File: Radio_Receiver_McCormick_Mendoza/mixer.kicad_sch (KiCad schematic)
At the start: 32 parts, among them J13 I_0, J14 I_180, J15 Q_90, J16 Q_270, J17 I_OUT, J18 Conn_01x02_Female, J19 Conn_01x02_Female, J20 Q_OUT, U11 INA821ID, U8 SN74CBT3253CDBR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

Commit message: Isolated filter switching MUX from digital control
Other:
- moved on the sheet: J18, J19
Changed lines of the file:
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@@
 	)
 	(junction
-		(at 176.53 54.61)
+		(at 138.43 43.18)
 		(diameter 0)
 		(color 0 0 0 0)
 	)
 	(junction
-		(at 187.96 133.35)
+		(at 134.62 91.44)
 		(diameter 0)
 		(color 0 0 0 0)
 	)
 	(junction
-		(at 138.43 43.18)
+		(at 261.62 59.69)
 		(diameter 0)
 		(color 0 0 0 0)
 	)
 	(junction
-		(at 134.62 91.44)
+		(at 176.53 54.61)
 		(diameter 0)
 		(color 0 0 0 0)
 	)
 	(junction
-		(at 261.62 59.69)
+		(at 186.69 71.12)
 		(diameter 0)
 		(color 0 0 0 0)
@@
 	)
 	(junction
-		(at 177.8 116.84)
+		(at 194.31 116.84)
 		(diameter 0)
 		(color 0 0 0 0)
 	)
 	(junction
-		(at 194.31 116.84)
+		(at 137.16 93.98)
 		(diameter 0)
 		(color 0 0 0 0)
 	)
 	(junction
-		(at 137.16 93.98)
+		(at 187.96 133.35)
 		(diameter 0)
 		(color 0 0 0 0)
@@
 	)
 	(junction
+		(at 177.8 116.84)
+		(diameter 0)
+		(color 0 0 0 0)
+	)
+	(junction
 		(at 203.2 71.12)
 		(diameter 0)
@@
 	)
 	(junction
-		(at 186.69 71.12)
-		(diameter 0)
-		(color 0 0 0 0)
-	)
-	(junction
 		(at 139.7 83.82)
 		(diameter 0)
@@
 	(wire
 		(pts
-			(xy 154.94 68.58) (xy 154.94 54.61)
+			(xy 172.72 62.23) (xy 172.72 54.61)
 		)
 		(stroke
@@
 	(wire
 		(pts
+			(xy 173.99 125.73) (xy 173.99 133.35)
+		)
+		(stroke
+			(width 0)
+			(type default)
+		)
+	)
+	(wire
+		(pts
 			(xy 137.16 143.51) (xy 168.91 143.51)
 		)
@@
 	(wire
 		(pts
-			(xy 154.94 130.81) (xy 156.21 130.81)
+			(xy 172.72 123.19) (xy 173.99 123.19)
 		)
 		(stroke
@@
 	(wire
 		(pts
+			(xy 172.72 64.77) (xy 172.72 71.12)
+		)
+		(stroke
+			(width 0)
+			(type default)
+		)
+	)
+	(wire
+		(pts
 			(xy 245.11 130.81) (xy 246.38 130.81)
 		)
@@
 	(wire
 		(pts
-			(xy 153.67 71.12) (xy 186.69 71.12)
+			(xy 167.64 64.77) (xy 172.72 64.77)
 		)
 		(stroke
@@
 	(wire
 		(pts
-			(xy 154.94 54.61) (xy 176.53 54.61)
+			(xy 172.72 54.61) (xy 176.53 54.61)
 		)
 		(stroke
@@
 	(wire
 		(pts
+			(xy 172.72 71.12) (xy 186.69 71.12)
+		)
+		(stroke
+			(width 0)
+			(type default)
+		)
+	)
+	(wire
+		(pts
 			(xy 232.41 143.51) (xy 232.41 128.27)
 		)
@@
 	(wire
 		(pts
+			(xy 173.99 133.35) (xy 187.96 133.35)
+		)
+		(stroke
+			(width 0)
+			(type default)
+		)
+	)
+	(wire
+		(pts
 			(xy 261.62 115.57) (xy 271.78 115.57)
 		)
@@
 	(wire
 		(pts
-			(xy 153.67 68.58) (xy 154.94 68.58)
+			(xy 167.64 62.23) (xy 172.72 62.23)
 		)
 		(stroke
@@
 	(wire
 		(pts
-			(xy 156.21 130.81) (xy 156.21 116.84)
+			(xy 173.99 123.19) (xy 173.99 116.84)
 		)
 		(stroke
@@
 	(wire
 		(pts
-			(xy 154.94 133.35) (xy 187.96 133.35)
+			(xy 172.72 125.73) (xy 173.99 125.73)
 		)
 		(stroke
@@
 	(wire
 		(pts
-			(xy 156.21 116.84) (xy 177.8 116.84)
+			(xy 173.99 116.84) (xy 177.8 116.84)
 		)
 		(stroke
@@
 	(symbol
 		(lib_id "Connector:Conn_01x02_Female")
-		(at 149.86 133.35 180)
+		(at 167.64 125.73 180)
 		(unit 1)
 		(body_style 1)
@@
 		(dnp no)
 		(property "Reference" "J19"
-			(at 146.304 132.842 0)
+			(at 164.084 125.222 0)
 			(show_name no)
 			(do_not_autoplace no)
@@
 		)
 		(property "Value" "Conn_01x02_Female"
-			(at 147.574 135.382 0)
+			(at 165.354 127.762 0)
 			(show_name no)
 			(do_not_autoplace no)
@@
 		)
 		(property "Footprint" "Connector_PinSocket_2.54mm:PinSocket_1x02_P2.54mm_Vertical"
-			(at 149.86 133.35 0)
+			(at 167.64 125.73 0)
 			(hide yes)
 			(show_name no)
@@
 		)
 		(property "Datasheet" "~"
-			(at 149.86 133.35 0)
+			(at 167.64 125.73 0)
 			(hide yes)
 			(show_name no)
@@
 		)
 		(property "Description" ""
-			(at 149.86 133.35 0)
+			(at 167.64 125.73 0)
 			(show_name no)
 			(do_not_autoplace no)
@@
 	(symbol
 		(lib_id "Connector:Conn_01x02_Female")
-		(at 148.59 71.12 180)
+		(at 162.56 64.77 180)
 		(unit 1)
 		(body_style 1)
@@
 		(dnp no)
 		(property "Reference" "J18"
-			(at 145.034 70.612 0)
+			(at 159.004 64.262 0)
 			(show_name no)
 			(do_not_autoplace no)
@@
 		)
 		(property "Value" "Conn_01x02_Female"
-			(at 146.304 73.152 0)
+			(at 160.274 66.802 0)
 			(show_name no)
 			(do_not_autoplace no)
@@
 		)
 		(property "Footprint" "Connector_PinSocket_2.54mm:PinSocket_1x02_P2.54mm_Vertical"
-			(at 148.59 71.12 0)
+			(at 162.56 64.77 0)
 			(hide yes)
 			(show_name no)
@@
 		)
 		(property "Datasheet" "~"
-			(at 148.59 71.12 0)
+			(at 162.56 64.77 0)
 			(hide yes)
 			(show_name no)
@@
 		)
 		(property "Description" ""
-			(at 148.59 71.12 0)
+			(at 162.56 64.77 0)
 			(show_name no)
 			(do_not_autoplace no)

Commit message: Added digital power regulator
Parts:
- removed C19, C21: 100nF, PCM_JLCPCB:C_1206, symbol Device:C
- added C62, C63: 100nF, PCM_JLCPCB:C_1206, symbol Device:C
- C14, C15, C9: Manufacturer Samsung Electro-Mechanics -> (none)
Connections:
- net GND: now also C62.2, C63.2
- net VDDA/2: now also C62.1, C63.1
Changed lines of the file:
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@@
 	)
 	(symbol
-		(lib_id "Device:C")
-		(at 246.38 138.43 0)
-		(unit 1)
-		(body_style 1)
-		(exclude_from_sim no)
-		(in_bom yes)
-		(on_board yes)
-		(in_pos_files yes)
-		(dnp no)
-		(fields_autoplaced yes)
-		(property "Reference" "C19"
-			(at 250.19 137.1599 0)
-			(show_name no)
-			(do_not_autoplace no)
-			(effects
-				(font
-					(size 1.27 1.27)
-				)
-				(justify left)
-			)
-		)
-		(property "Value" "100nF"
-			(at 250.19 139.6999 0)
-			(show_name no)
-			(do_not_autoplace no)
-			(effects
-				(font
-					(size 1.27 1.27)
-				)
-				(justify left)
-			)
-		)
-		(property "Footprint" "PCM_JLCPCB:C_1206"
-			(at 247.3452 142.24 0)
-			(hide yes)
-			(show_name no)
-			(do_not_autoplace no)
-			(effects
-				(font
-					(size 1.27 1.27)
-				)
-			)
-		)
-		(property "Datasheet" "https://jlcpcb.com/partdetail/HRE-CSA1206C0G104J500NT/C52147198"
-			(at 246.38 138.43 0)
-			(hide yes)
-			(show_name no)
-			(do_not_autoplace no)
-			(effects
-				(font
-					(size 1.27 1.27)
-				)
-			)
-		)
-		(property "Description" "100nF 50V C0G ±5% 1206 Multilayer Ceramic Capacitors MLCC - SMD/SMT ROHS"
-			(at 246.38 138.43 0)
-			(hide yes)
-			(show_name no)
-			(do_not_autoplace no)
-			(effects
-				(font
-					(size 1.27 1.27)
-				)
-			)
-		)
-		(pin "2"
-		)
-		(pin "1"
-		)
-		(instances
-			(project "Radio_Receiver_McCormick_Mendoza"
-				(path "/f31d31ab-6846-4f3a-92b1-aa5a6a13373f/132a78a3-63a8-4709-a5ba-2b34eb7966d9"
-					(reference "C19")
-					(unit 1)
-				)
-			)
-		)
-	)
-	(symbol
 		(lib_id "Jumper:Jumper_2_Open")
 		(at 198.12 63.5 0)
@@
 			)
 		)
-		(property "Manufacturer" "Samsung Electro-Mechanics"
-			(at 63.5 64.77 0)
-			(hide yes)
-			(show_name no)
-			(do_not_autoplace no)
-			(effects
-				(font
-					(size 1.27 1.27)
-				)
-			)
-		)
 		(property "Part" "CL21B104KCFNNNE"
 			(at 63.5 64.77 0)
@@
 	)
 	(symbol
-		(lib_id "Device:C")
-		(at 245.11 74.93 0)
-		(unit 1)
-		(body_style 1)
-		(exclude_from_sim no)
-		(in_bom yes)
-		(on_board yes)
-		(in_pos_files yes)
-		(dnp no)
-		(fields_autoplaced yes)
-		(property "Reference" "C21"
-			(at 248.92 73.6599 0)
-			(show_name no)
-			(do_not_autoplace no)
-			(effects
-				(font
-					(size 1.27 1.27)
-				)
-				(justify left)
-			)
-		)
-		(property "Value" "100nF"
-			(at 248.92 76.1999 0)
-			(show_name no)
-			(do_not_autoplace no)
-			(effects
-				(font
-					(size 1.27 1.27)
-				)
-				(justify left)
-			)
-		)
-		(property "Footprint" "PCM_JLCPCB:C_1206"
-			(at 246.0752 78.74 0)
-			(hide yes)
-			(show_name no)
-			(do_not_autoplace no)
-			(effects
-				(font
-					(size 1.27 1.27)
-				)
-			)
-		)
-		(property "Datasheet" "https://jlcpcb.com/partdetail/HRE-CSA1206C0G104J500NT/C52147198"
-			(at 245.11 74.93 0)
-			(hide yes)
-			(show_name no)
-			(do_not_autoplace no)
-			(effects
-				(font
-					(size 1.27 1.27)
-				)
-			)
-		)
-		(property "Description" "100nF 50V C0G ±5% 1206 Multilayer Ceramic Capacitors MLCC - SMD/SMT ROHS"
-			(at 245.11 74.93 0)
-			(hide yes)
-			(show_name no)
-			(do_not_autoplace no)
-			(effects
-				(font
-					(size 1.27 1.27)
-				)
-			)
-		)
-		(pin "2"
-		)
-		(pin "1"
-		)
-		(instances
-			(project "Radio_Receiver_McCormick_Mendoza"
-				(path "/f31d31ab-6846-4f3a-92b1-aa5a6a13373f/132a78a3-63a8-4709-a5ba-2b34eb7966d9"
-					(reference "C21")
-					(unit 1)
-				)
-			)
-		)
-	)
-	(symbol
 		(lib_id "Connector:Conn_01x02_Female")
 		(at 167.64 125.73 180)
@@
 	)
 	(symbol
+		(lib_id "Device:C")
+		(at 246.38 138.43 0)
+		(unit 1)
+		(body_style 1)
+		(exclude_from_sim no)
+		(in_bom yes)
+		(on_board yes)
+		(in_pos_files yes)
+		(dnp no)
+		(fields_autoplaced yes)
+		(property "Reference" "C63"
+			(at 250.19 137.1599 0)
+			(show_name no)
+			(do_not_autoplace no)
+			(effects
+				(font
+					(size 1.27 1.27)
+				)
+				(justify left)
+			)
+		)
+		(property "Value" "100nF"
+			(at 250.19 139.6999 0)
+			(show_name no)
+			(do_not_autoplace no)
+			(effects
+				(font
+					(size 1.27 1.27)
+				)
+				(justify left)
+			)
+		)
+		(property "Footprint" "PCM_JLCPCB:C_1206"
+			(at 247.3452 142.24 0)
+			(hide yes)
+			(show_name no)
+			(do_not_autoplace no)
+			(effects
+				(font
+					(size 1.27 1.27)
+				)
+			)
+		)
+		(property "Datasheet" "https://jlcpcb.com/partdetail/HRE-CSA1206C0G104J500NT/C52147198"
+			(at 246.38 138.43 0)
+			(hide yes)
+			(show_name no)
+			(do_not_autoplace no)
+			(effects
+				(font
+					(size 1.27 1.27)
+				)
+			)
+		)
+		(property "Description" "100nF 50V C0G ±5% 1206 Multilayer Ceramic Capacitors MLCC - SMD/SMT ROHS"
+			(at 246.38 138.43 0)
+			(hide yes)
+			(show_name no)
+			(do_not_autoplace no)
+			(effects
+				(font
+					(size 1.27 1.27)
+				)
+			)
+		)
+		(property "LCSC" "C52147198"
+			(at 246.38 138.43 0)
+			(hide yes)
+			(show_name no)
+			(do_not_autoplace no)
+			(effects
+				(font
+					(size 1.27 1.27)
+				)
+			)
+		)
+		(pin "2"
+		)
+		(pin "1"
+		)
+		(instances
+			(project "Radio_Receiver_McCormick_Mendoza"
+				(path "/f31d31ab-6846-4f3a-92b1-aa5a6a13373f/132a78a3-63a8-4709-a5ba-2b34eb7966d9"
+					(reference "C63")
+					(unit 1)
+				)
+			)
+		)
+	)
+	(symbol
 		(lib_id "power:GND")
 		(at 115.57 106.68 0)
@@
 			)
 		)
-		(property "Manufacturer" "Samsung Electro-Mechanics"
-			(at 245.11 49.53 0)
-			(hide yes)
-			(show_name no)
-			(do_not_autoplace no)
-			(effects
-				(font
-					(size 1.27 1.27)
-				)
-			)
-		)
 		(property "Part" "CL21B104KCFNNNE"
 			(at 245.11 49.53 0)
@@
 	(symbol
 		(lib_id "Device:C")
+		(at 245.11 74.93 0)
+		(unit 1)
+		(body_style 1)
+		(exclude_from_sim no)
+		(in_bom yes)
+		(on_board yes)
+		(in_pos_files yes)
+		(dnp no)
+		(fields_autoplaced yes)
+		(property "Reference" "C62"
+			(at 248.92 73.6599 0)
+			(show_name no)
+			(do_not_autoplace no)
+			(effects
+				(font
+					(size 1.27 1.27)
+				)
+				(justify left)
+			)
+		)
+		(property "Value" "100nF"
+			(at 248.92 76.1999 0)
+			(show_name no)
+			(do_not_autoplace no)
+			(effects
+				(font
+					(size 1.27 1.27)
+				)
+				(justify left)
+			)
+		)
+		(property "Footprint" "PCM_JLCPCB:C_1206"
+			(at 246.0752 78.74 0)
+			(hide yes)
+			(show_name no)
+			(do_not_autoplace no)
+			(effects
+				(font
+					(size 1.27 1.27)
+				)
+			)
+		)
+		(property "Datasheet" "https://jlcpcb.com/partdetail/HRE-CSA1206C0G104J500NT/C52147198"
+			(at 245.11 74.93 0)
+			(hide yes)
+			(show_name no)
+			(do_not_autoplace no)
+			(effects
+				(font
+					(size 1.27 1.27)
+				)
+			)
+		)
+		(property "Description" "100nF 50V C0G ±5% 1206 Multilayer Ceramic Capacitors MLCC - SMD/SMT ROHS"
+			(at 245.11 74.93 0)
+			(hide yes)
+			(show_name no)
+			(do_not_autoplace no)
+			(effects
+				(font
+					(size 1.27 1.27)
+				)
+			)
+		)
+		(property "LCSC" "C52147198"
+			(at 245.11 74.93 0)
+			(hide yes)
+			(show_name no)
+			(do_not_autoplace no)
+			(effects
+				(font
+					(size 1.27 1.27)
+				)
+			)
+		)
+		(pin "2"
+		)
+		(pin "1"
+		)
+		(instances
+			(project "Radio_Receiver_McCormick_Mendoza"
+				(path "/f31d31ab-6846-4f3a-92b1-aa5a6a13373f/132a78a3-63a8-4709-a5ba-2b34eb7966d9"
+					(reference "C62")
+					(unit 1)
+				)
+			)
+		)
+	)
+	(symbol
+		(lib_id "Device:C")
 		(at 138.43 46.99 0)
 		(unit 1)
@@
 			(at 246.38 113.03 0)
 			(hide yes)
-			(show_name no)
-			(do_not_autoplace no)
-			(effects
-				(font
-					(size 1.27 1.27)
-				)
-			)
-		)
-		(property "Manufacturer" "Samsung Electro-Mechanics"
-			(at 246.38 113.03 0)
-			(hide yes)

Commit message: Integrated signal path modules
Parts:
- removed C10, C11, C17, C18: 100p, Capacitor_THT:C_Disc_D5.0mm_W2.5mm_P2.50mm, symbol Device:C
- added C69, C79, C81, C82: 10nF, PCM_JLCPCB:C_0805, symbol Device:C
- J17: value I_OUT -> I_RAW
- J20: value Q_OUT -> Q_RAW
- R11, R14: LCSC (none) -> C861188
- R12, R15: LCSC (none) -> C861486
- R13, R16: LCSC (none) -> C861101
- U11, U9: LCSC (none) -> C2060822
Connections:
- net 00 = 0°: now also C69.2
- net 01 = 270°: now also C82.2
- net 10 = 90°: now also C81.2
- net 11 = 180°: now also C79.2
- net GND: now also C69.1, C79.1, C81.1, C82.1

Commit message: Finalized Pico connections and added indicator LEDs
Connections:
- net BPF_OUT1 renamed RF_IN1
- net BPF_OUT2 renamed RF_IN2

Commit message: Added transformer footprint and datasheet
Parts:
- U8: LCSC (none) -> C2674583; Price (none) -> 3.5033USD
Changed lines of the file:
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@@
+			)
+		)
+		(property "LCSC" "C2674583"
+			(at 95.25 88.9 0)
+			(hide yes)
+			(show_name no)
+			(do_not_autoplace no)
+			(effects
+				(font
+					(size 1.27 1.27)
+				)
+			)
+		)
+		(property "Price" "3.5033USD"
+			(at 95.25 88.9 0)
+			(hide yes)
+			(show_name no)
+			(do_not_autoplace no)
+			(effects
+				(font
+					(size 1.27 1.27)
+				)
 			)
 		)

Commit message: Added MicroSD card and verified footprints
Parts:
- JP2, JP3, JP4, JP7, JP8, JP9: footprint (none) -> Jumper:SolderJumper-2_P1.3mm_Open_RoundedPad1.0x1.5mm
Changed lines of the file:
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@@
 			)
 		)
-		(property "Footprint" ""
+		(property "Footprint" "Jumper:SolderJumper-2_P1.3mm_Open_RoundedPad1.0x1.5mm"
 			(at 182.88 125.73 0)
 			(hide yes)
@@
 			)
 		)
-		(property "Footprint" ""
+		(property "Footprint" "Jumper:SolderJumper-2_P1.3mm_Open_RoundedPad1.0x1.5mm"
 			(at 198.12 63.5 0)
 			(hide yes)
@@
 			)
 		)
-		(property "Footprint" ""
+		(property "Footprint" "Jumper:SolderJumper-2_P1.3mm_Open_RoundedPad1.0x1.5mm"
 			(at 214.63 63.5 0)
 			(hide yes)
@@
 			)
 		)
-		(property "Footprint" ""
+		(property "Footprint" "Jumper:SolderJumper-2_P1.3mm_Open_RoundedPad1.0x1.5mm"
 			(at 199.39 125.73 0)
 			(hide yes)
@@
 			)
 		)
-		(property "Footprint" ""
+		(property "Footprint" "Jumper:SolderJumper-2_P1.3mm_Open_RoundedPad1.0x1.5mm"
 			(at 215.9 125.73 0)
 			(hide yes)
@@
 		(property "Description" ""
 			(at 190.5 83.82 0)
+			(hide yes)
 			(show_name no)
 			(do_not_autoplace no)
@@
 			)
 		)
-		(property "Footprint" ""
+		(property "Footprint" "Jumper:SolderJumper-2_P1.3mm_Open_RoundedPad1.0x1.5mm"
 			(at 181.61 63.5 0)
 			(hide yes)

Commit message: Updated footprints
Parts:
- U11, U9: footprint import_footprint:SOIC127P600X175-8N -> INA821ID:D0008A_N
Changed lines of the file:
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@@
 	(wire
 		(pts
-			(xy 238.76 50.8) (xy 238.76 49.53)
-		)
-		(stroke
-			(width 0)
-			(type default)
-		)
-	)
-	(wire
-		(pts
 			(xy 219.71 71.12) (xy 228.6 71.12)
 		)
@@
 			)
 		)
-		(property "Footprint" "import_footprint:SOIC127P600X175-8N"
+		(property "Footprint" "INA821ID:D0008A_N"
 			(at 242.57 123.19 0)
 			(hide yes)
@@
 			)
 		)
-		(property "Footprint" "import_footprint:SOIC127P600X175-8N"
+		(property "Footprint" "INA821ID:D0008A_N"
 			(at 241.3 59.69 0)
 			(hide yes)

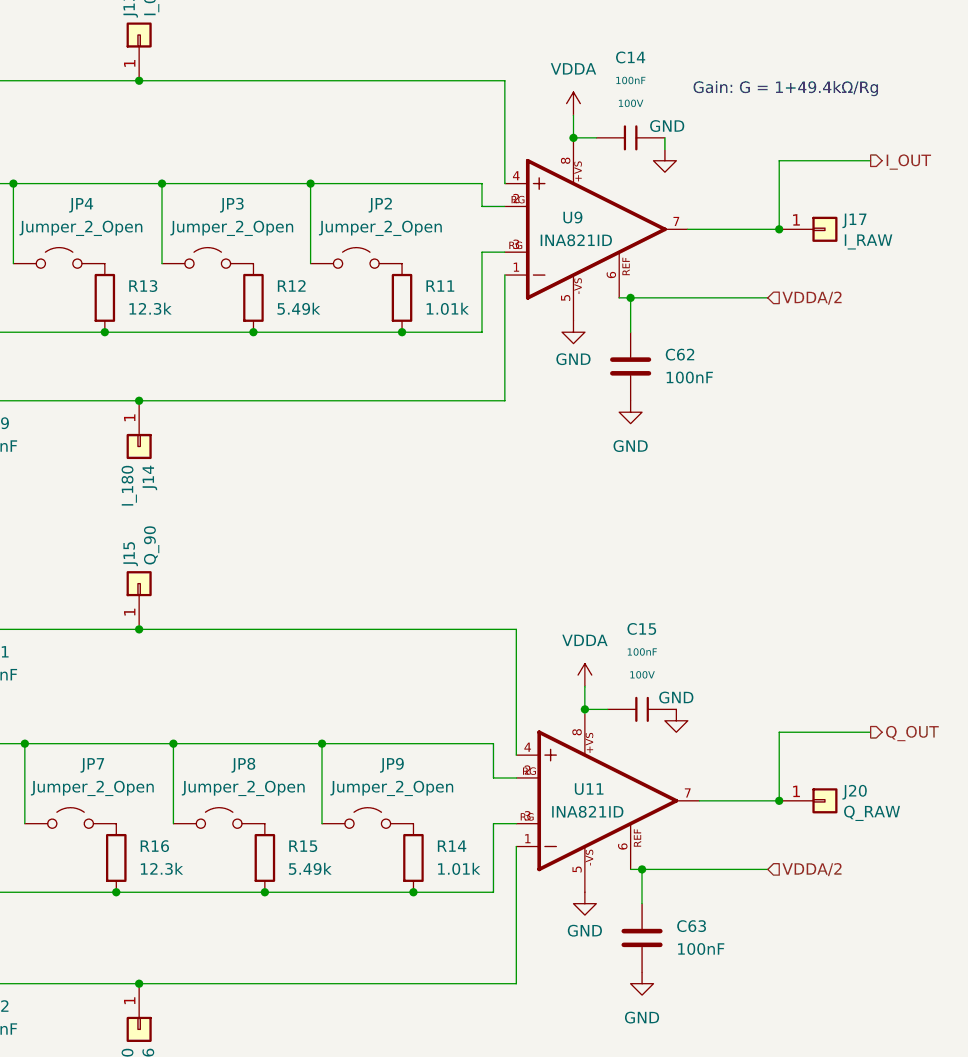
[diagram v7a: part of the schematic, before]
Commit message: Routed antenna and isolated GNDA
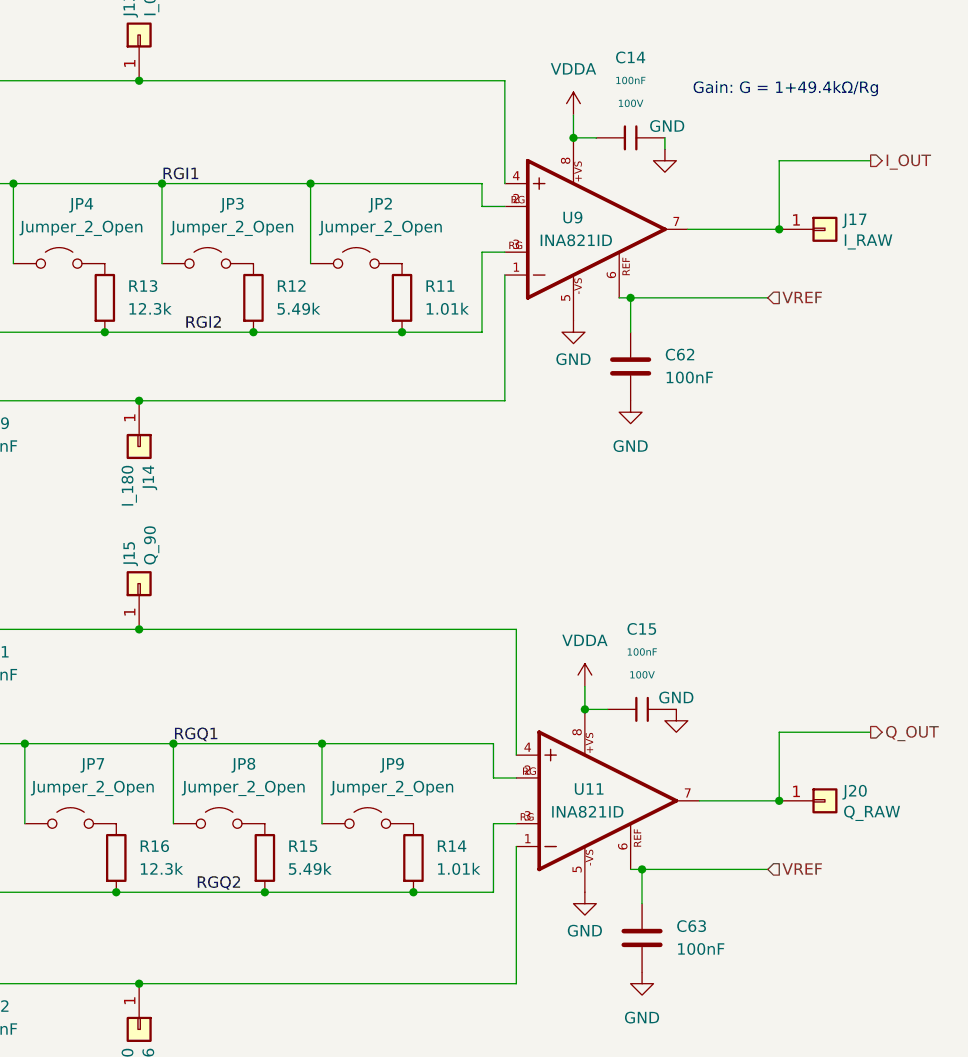
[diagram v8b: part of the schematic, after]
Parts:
- U11, U9: footprint INA821ID:D0008A_N -> Reciever_Parts:D0008A_N
- U8: footprint SN74CBT3253CDBR_1-4_MUX:DB0016A_N -> Reciever_Parts:DB0016A_N
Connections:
- net RGQ2: now reaches J19.1 (Pin_1), R14.2, R15.2, R16.2, U11.3 (RG1)
- net RGQ1: now reaches J19.2 (Pin_2), JP7.1 (A), JP8.1 (A), JP9.1 (A), U11.2 (RG)
- net RGI1: now reaches J18.2 (Pin_2), JP2.1 (A), JP3.1 (A), JP4.1 (A), U9.2 (RG)
- net RGI2: now reaches J18.1 (Pin_1), R11.2, R12.2, R13.2, U9.3 (RG1)
- net VDDA/2 renamed VREF
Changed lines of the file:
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@@
 		)
 	)
+	(label "RGI1"
+		(at 193.04 54.61 0)
+		(effects
+			(font
+				(size 1.27 1.27)
+			)
+			(justify left bottom)
+		)
+	)
 	(label "00 = 0°"
 		(at 125.73 76.2 180)
@@
 		)
 	)
+	(label "RGQ1"
+		(at 194.31 116.84 0)
+		(effects
+			(font
+				(size 1.27 1.27)
+			)
+			(justify left bottom)
+		)
+	)
 	(label "11 = 180°"
 		(at 156.21 78.74 180)
@@
 		)
 	)
+	(label "RGI2"
+		(at 195.58 71.12 0)
+		(effects
+			(font
+				(size 1.27 1.27)
+			)
+			(justify left bottom)
+		)
+	)
+	(label "RGQ2"
+		(at 196.85 133.35 0)
+		(effects
+			(font
+				(size 1.27 1.27)
+			)
+			(justify left bottom)
+		)
+	)
 	(label "01 = 270°"
 		(at 127 81.28 180)
@@
 		)
 	)
-	(hierarchical_label "VDDA{slash}2"
+	(hierarchical_label "VREF"
 		(shape input)
 		(at 260.35 130.81 0)
@@
 		)
 	)
-	(hierarchical_label "VDDA{slash}2"
+	(hierarchical_label "VREF"
 		(shape input)
 		(at 260.35 67.31 0)
@@
 			)
 		)
-		(property "Footprint" "INA821ID:D0008A_N"
+		(property "Footprint" "Reciever_Parts:D0008A_N"
 			(at 242.57 123.19 0)
 			(hide yes)
@@
 			)
 		)
-		(property "Footprint" "SN74CBT3253CDBR_1-4_MUX:DB0016A_N"
+		(property "Footprint" "Reciever_Parts:DB0016A_N"
 			(at 95.25 88.9 0)
 			(hide yes)
@@
 			)
 		)
-		(property "Footprint" "INA821ID:D0008A_N"
+		(property "Footprint" "Reciever_Parts:D0008A_N"
 			(at 241.3 59.69 0)
 			(hide yes)
